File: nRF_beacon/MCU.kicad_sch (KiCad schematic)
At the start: 11 parts, among them U1 nRF54L15, X1 32MHz

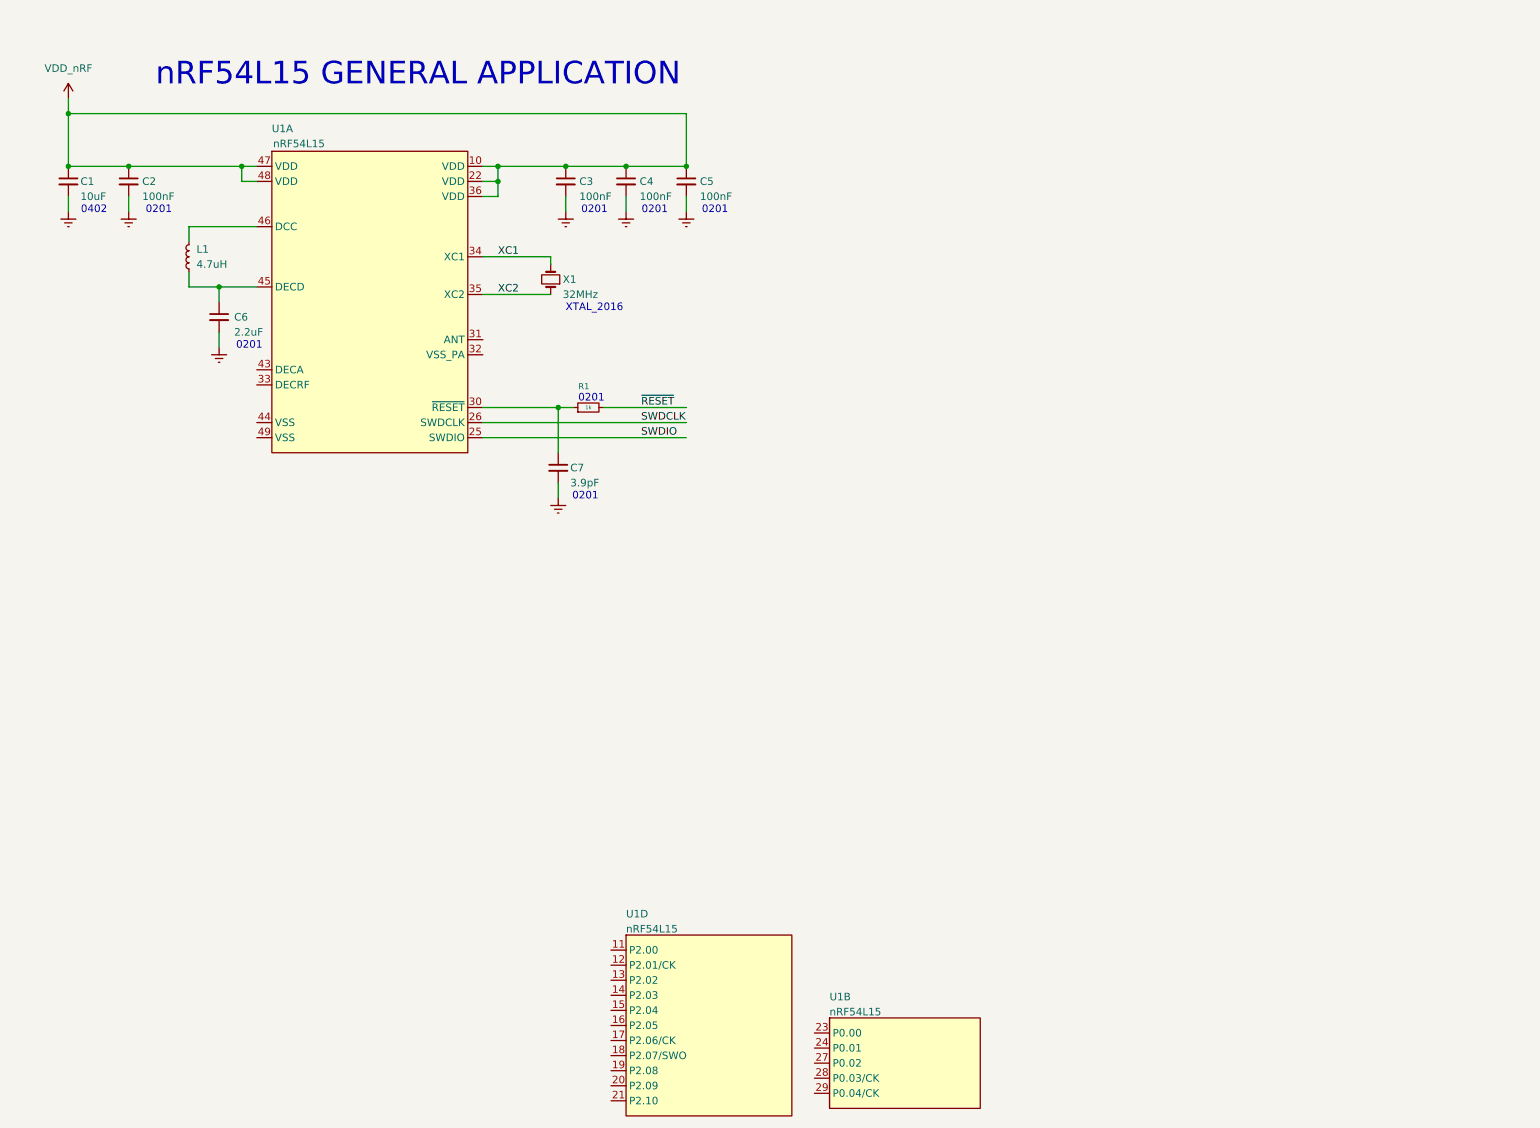
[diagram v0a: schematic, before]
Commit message: Finished typical application nRF. Added audio-block in root sheet.
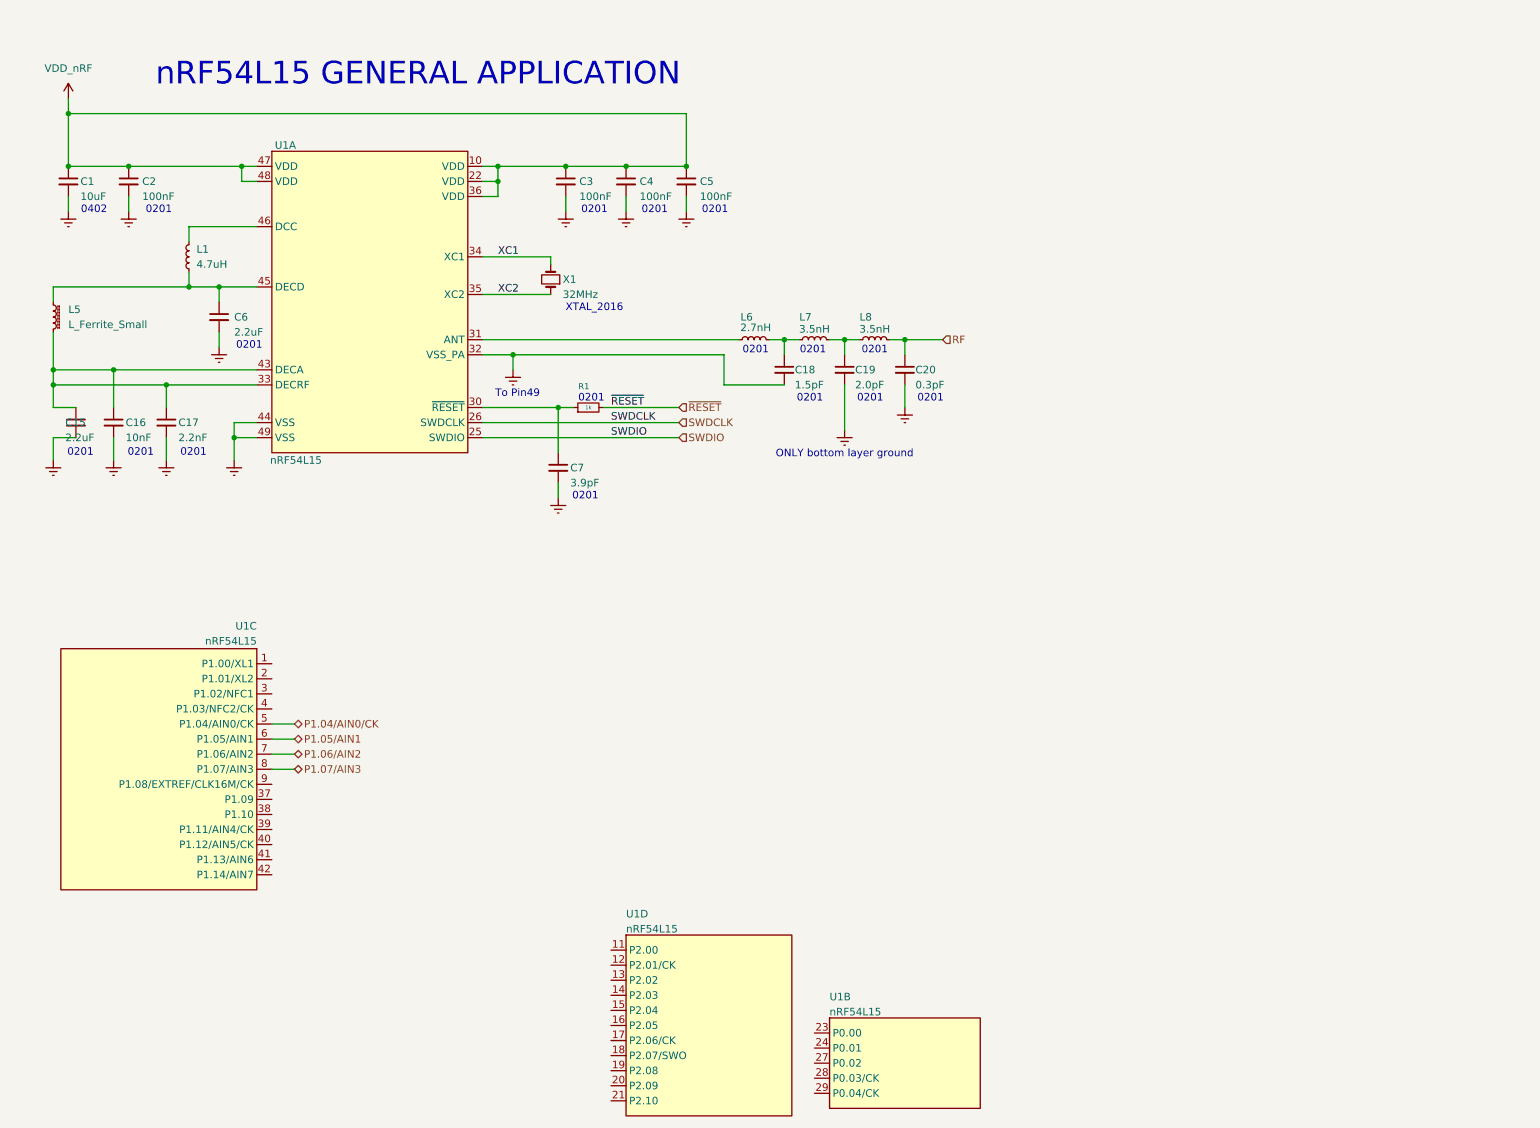
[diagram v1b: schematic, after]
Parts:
- added C15: 2.2uF, symbol Device:C_Small
- added C16: 10nF, symbol Device:C_Small
- added C17: 2.2nF, symbol Device:C_Small
- added C18: 1.5pF, symbol Device:C_Small
- added C19: 2.0pF, symbol Device:C_Small
- added C20: 0.3pF, symbol Device:C_Small
- added L5: L_Ferrite_Small, symbol Device:L_Ferrite_Small
- added L6: 2.7nH, symbol Device:L_Small
- added L7, L8: 3.5nH, symbol Device:L_Small
- added unit 3 of U1
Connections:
- net Earth: now also U1.32 (VSS_PA), U1.44 (VSS), U1.49 (VSS), C15.2, C16.2, C17.2, C18.2, C19.2, C20.2
- net at C6.1, L1.1, U1.45 (DECD): now also L5.1
- net at U1.31 (ANT): now also L6.1
- net at U1.33 (DECRF): now also U1.43 (DECA), C15.1, C16.1, C17.1, L5.2
- new net: C18.1, L6.2, L7.1
- new net: C19.1, L7.2, L8.1
- new net P1.04/AIN0/CK: U1.5 (P1.04/AIN0/CK)
- new net P1.05/AIN1: U1.6 (P1.05/AIN1)
- new net P1.06/AIN2: U1.7 (P1.06/AIN2)
- new net P1.07/AIN3: U1.8 (P1.07/AIN3)
- new net RF: C20.1, L8.2
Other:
- note added: "ONLY bottom layer ground"
- note added: "To Pin49"

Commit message: Added MPN and footprints for all components on nRF general application
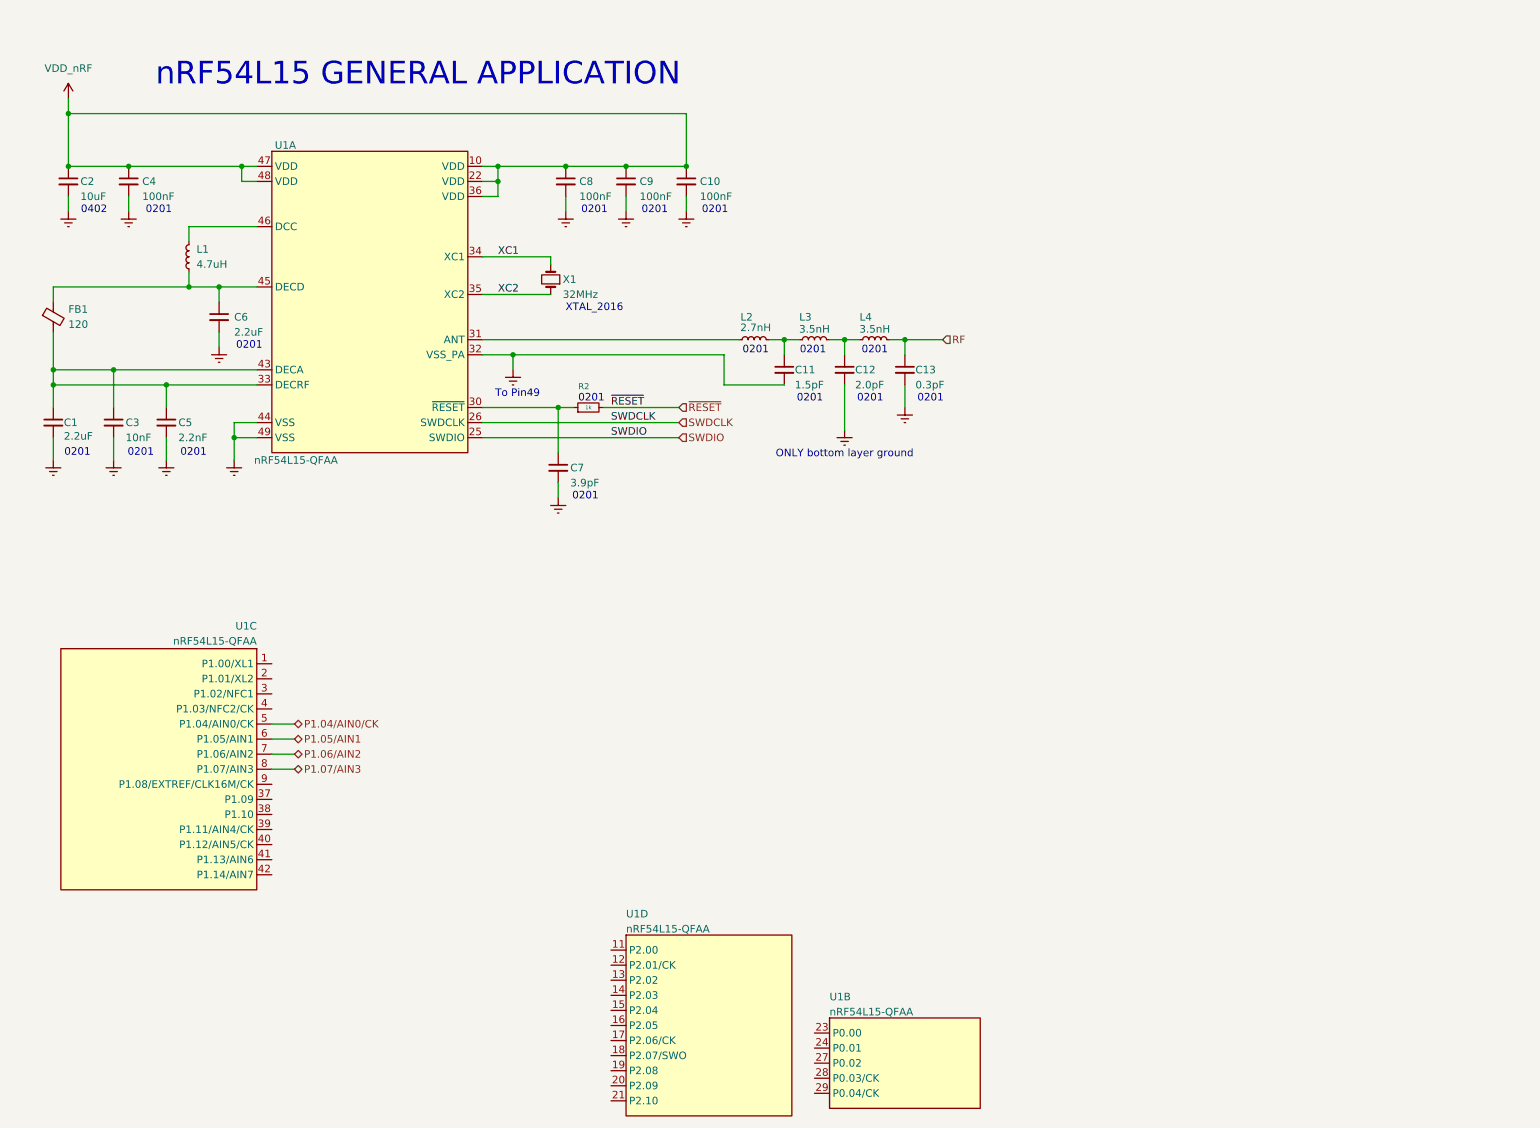
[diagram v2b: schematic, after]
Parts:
- removed L5: L_Ferrite_Small, symbol Device:L_Ferrite_Small
- added FB1: 120, Inductor_SMD:L_0201_0603Metric_Pad0.64x0.40mm_HandSolder, symbol Device:FerriteBead_Small
- C1: renamed from C15; footprint (none) -> Capacitor_SMD:C_0201_0603Metric_Pad0.64x0.40mm_HandSolder; MPN (none) -> GRM033D80E225ME47D; Price (none) -> 1.10
- C10: renamed from C5; footprint (none) -> Capacitor_SMD:C_0201_0603Metric_Pad0.64x0.40mm_HandSolder; MPN (none) -> KGM03AR70J104KH; Price (none) -> 3.6
- C11: renamed from C18; footprint (none) -> Capacitor_SMD:C_0201_0603Metric_Pad0.64x0.40mm_HandSolder; MPN (none) -> GJM0335C1E1R5WB01J; Price (none) -> 0.998
- C12: renamed from C19; footprint (none) -> Capacitor_SMD:C_0201_0603Metric_Pad0.64x0.40mm_HandSolder; MPN (none) -> GJM0335C1E2R0WB01D; Price (none) -> 1.19
- C13: renamed from C20; footprint (none) -> Capacitor_SMD:C_0201_0603Metric_Pad0.64x0.40mm_HandSolder; MPN (none) -> GCQ0335C1HR30BB01D; Price (none) -> 1.19
- C2: renamed from C1; footprint (none) -> Capacitor_SMD:C_0402_1005Metric_Pad0.74x0.62mm_HandSolder; MPN (none) -> KGM05CS60J106MH; Price (none) -> 3.19
- C3: renamed from C16; footprint (none) -> Capacitor_SMD:C_0201_0603Metric_Pad0.64x0.40mm_HandSolder; MPN (none) -> GRM033R70J103JA01D; Price (none) -> 0.998
- C4: renamed from C2; footprint (none) -> Capacitor_SMD:C_0201_0603Metric_Pad0.64x0.40mm_HandSolder; MPN (none) -> KGM03AR70J104KH; Price (none) -> 3.6
- C5: renamed from C17; footprint (none) -> Capacitor_SMD:C_0201_0603Metric_Pad0.64x0.40mm_HandSolder; MPN (none) -> GRM033R71A222KA01D; Price (none) -> 0.998
- C6: footprint (none) -> Capacitor_SMD:C_0201_0603Metric_Pad0.64x0.40mm_HandSolder; MPN (none) -> GRM033D80E225ME47D; Price (none) -> 1.10
- C7: footprint (none) -> Capacitor_SMD:C_0201_0603Metric_Pad0.64x0.40mm_HandSolder; MPN (none) -> GCQ0335C1H3R9CB01D; Price (none) -> 1.19
- C8: renamed from C3; footprint (none) -> Capacitor_SMD:C_0201_0603Metric_Pad0.64x0.40mm_HandSolder; MPN (none) -> KGM03AR70J104KH; Price (none) -> 3.6
- C9: renamed from C4; footprint (none) -> Capacitor_SMD:C_0201_0603Metric_Pad0.64x0.40mm_HandSolder; MPN (none) -> KGM03AR70J104KH; Price (none) -> 3.6
- L1: footprint (none) -> Inductor_SMD:L_0603_1608Metric_Pad1.05x0.95mm_HandSolder; MPN (none) -> LQM18PN4R7MFRL; Price (none) -> 1.69
- L2: renamed from L6; footprint (none) -> Inductor_SMD:L_0201_0603Metric_Pad0.64x0.40mm_HandSolder; MPN (none) -> LQP03HQ2N7B02D; Price (none) -> 1.19
- L3: renamed from L7; footprint (none) -> Inductor_SMD:L_0201_0603Metric_Pad0.64x0.40mm_HandSolder; MPN (none) -> LQP03HQ3N5B02D; Price (none) -> 1.19
- L4: renamed from L8; footprint (none) -> Inductor_SMD:L_0201_0603Metric_Pad0.64x0.40mm_HandSolder; MPN (none) -> LQP03HQ3N5B02D; Price (none) -> 1.19
- R2: renamed from R1; MPN (none) -> RCA02011K00FNEDSR; Price (none) -> 0.998
- U1: value nRF54L15 -> nRF54L15-QFAA; MPN (none) -> NRF54L15-QFAA-R7; Price (none) -> 23.08
- X1: footprint (none) -> Crystal:Crystal_SMD_2016-4Pin_2.0x1.6mm; MPN (none) -> CX2016DB32000D0WZRC1; Price (none) -> 6.59
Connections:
- net at C6.1, L1.1, U1.45 (DECD): now also FB1.1
- net at C1.1, C3.1, C5.1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: now also FB1.2
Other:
- moved on the sheet: C1

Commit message: Added buck configuration for AUDIO 3.3V power. Removed USB input
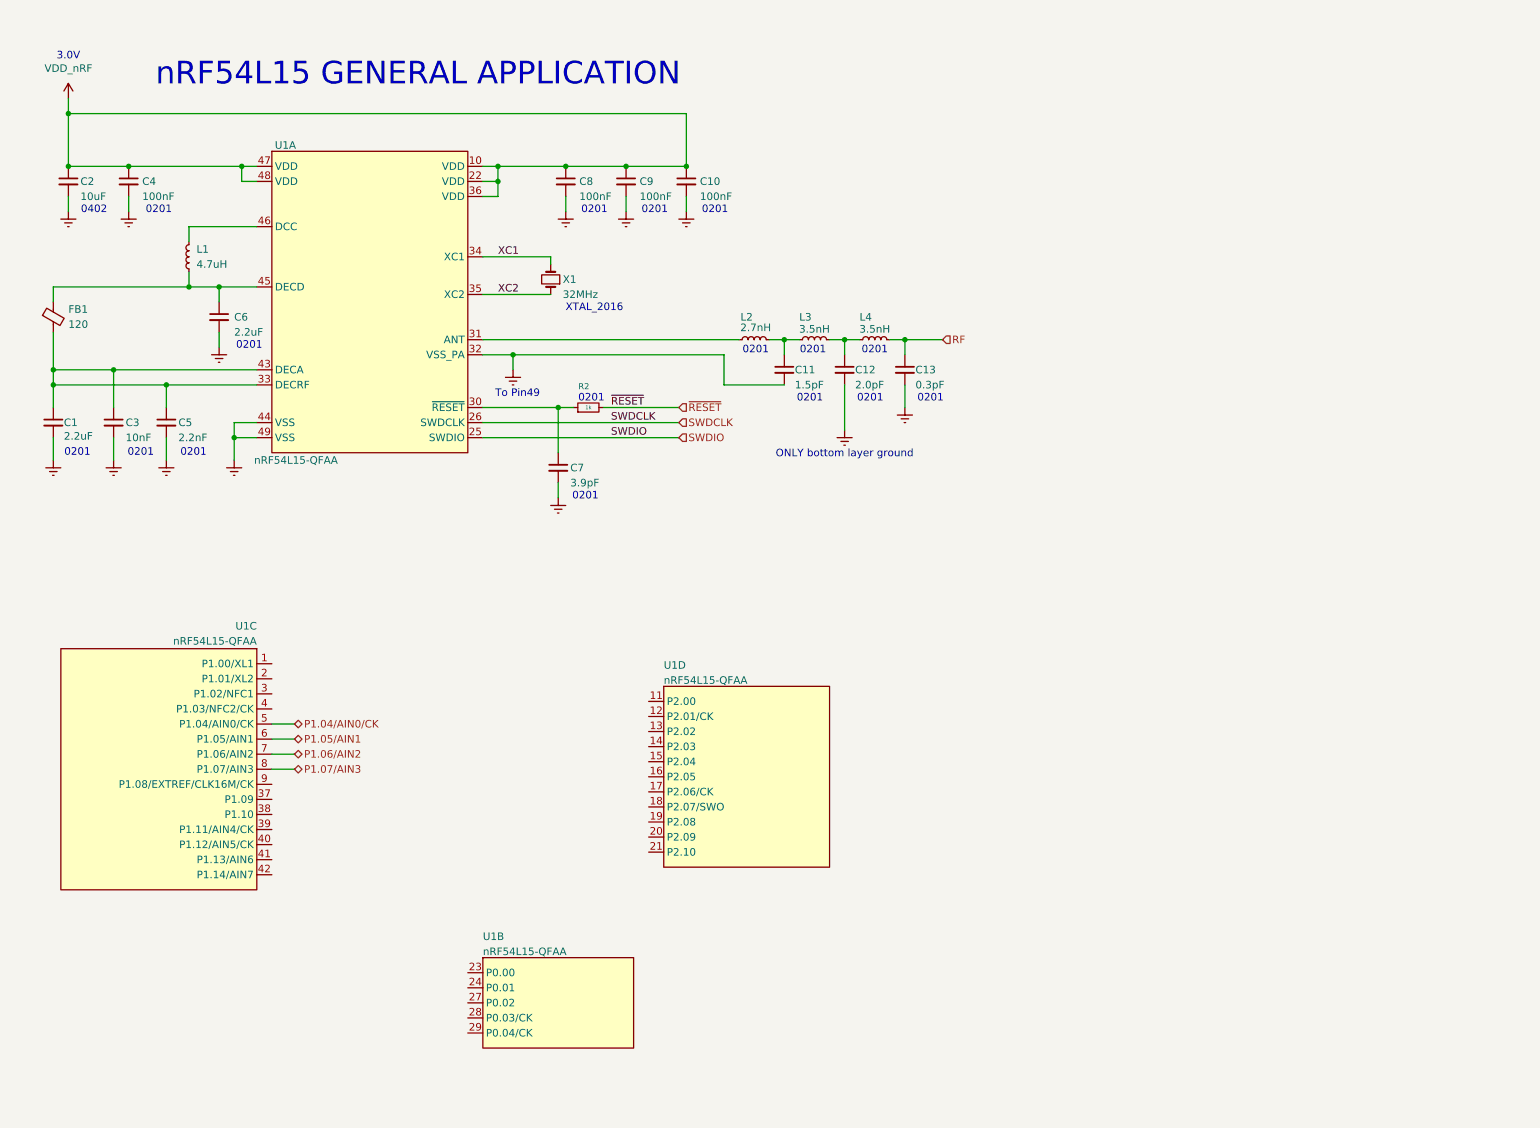
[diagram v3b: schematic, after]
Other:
- note added: "3.0V"
- moved on the sheet: U1B, U1D
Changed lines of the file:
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@@
 		)
 	)
+	(text "3.0V"
+		(exclude_from_sim no)
+		(at 21.59 19.558 0)
+		(effects
+			(font
+				(size 1.27 1.27)
+			)
+		)
+	)
 	(text "0201"
 		(exclude_from_sim no)
@@
 	(symbol
 		(lib_id "Ekse:nRF54L15")
-		(at 115.57 198.12 0)
+		(at 121.92 156.21 0)
 		(unit 4)
 		(exclude_from_sim no)
@@
 		(dnp no)
 		(property "Reference" "U1"
-			(at 115.57 164.084 0)
+			(at 121.92 122.174 0)
 			(effects
 				(font
@@
 		)
 		(property "Value" "nRF54L15-QFAA"
-			(at 115.57 166.624 0)
+			(at 121.92 124.714 0)
 			(effects
 				(font
@@
 		)
 		(property "Footprint" "Ekse:QFN48_6X6_NOR"
-			(at 115.57 198.12 0)
+			(at 121.92 156.21 0)
 			(effects
 				(font
@@
 		)
 		(property "Datasheet" ""
-			(at 115.57 198.12 0)
+			(at 121.92 156.21 0)
 			(effects
 				(font
@@
 		)
 		(property "Description" ""
-			(at 115.57 198.12 0)
+			(at 121.92 156.21 0)
 			(effects
 				(font
@@
 		)
 		(property "MPN" "NRF54L15-QFAA-R7"
-			(at 115.57 198.12 0)
+			(at 121.92 156.21 0)
 			(effects
 				(font
@@
 		)
 		(property "Price" "23.08"
-			(at 115.57 198.12 0)
+			(at 121.92 156.21 0)
 			(effects
 				(font
@@
 	(symbol
 		(lib_id "Ekse:nRF54L15")
-		(at 149.86 196.85 0)
+		(at 91.44 186.69 0)
 		(unit 2)
 		(exclude_from_sim no)
@@
 		(dnp no)
 		(property "Reference" "U1"
-			(at 149.86 178.054 0)
+			(at 91.44 167.894 0)
 			(effects
 				(font
@@
 		)
 		(property "Value" "nRF54L15-QFAA"
-			(at 149.86 180.594 0)
+			(at 91.44 170.434 0)
 			(effects
 				(font
@@
 		)
 		(property "Footprint" "Ekse:QFN48_6X6_NOR"
-			(at 149.86 196.85 0)
+			(at 91.44 186.69 0)
 			(effects
 				(font
@@
 		)
 		(property "Datasheet" ""
-			(at 149.86 196.85 0)
+			(at 91.44 186.69 0)
 			(effects
 				(font
@@
 		)
 		(property "Description" ""
-			(at 149.86 196.85 0)
+			(at 91.44 186.69 0)
 			(effects
 				(font
@@
 		)
 		(property "MPN" "NRF54L15-QFAA-R7"
-			(at 149.86 196.85 0)
+			(at 91.44 186.69 0)
 			(effects
 				(font
@@
 		)
 		(property "Price" "23.08"
-			(at 149.86 196.85 0)
+			(at 91.44 186.69 0)
 			(effects
 				(font
